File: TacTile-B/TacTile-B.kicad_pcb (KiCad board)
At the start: 2 copper layers, 59.9 x 59.9 mm, 97 parts, among them J1 Conn_01x02, J10 Conn_01x02, J11 Conn_01x02, J12 Conn_01x02, J13 Conn_01x02, J14 Conn_01x02, J15 Conn_01x02, J16 Conn_01x02, J17 Conn_01x02, J2 Conn_01x02, J3 Conn_01x02, J4 Conn_01x02, J5 Conn_01x02, J6 Conn_01x02, J7 Conn_01x02, J8 Conn_01x02, J9 Conn_01x02, U1 MCP14A0304xMNY, U10 MCP14A0304xMNY, U11 MCP14A0304xMNY, U12 MCP14A0304xMNY, U13 MCP14A0304xMNY, U14 MCP14A0304xMNY, U15 MCP14A0304xMNY, U16 MCP14A0304xMNY, U2 MCP14A0304xMNY, U3 MCP14A0304xMNY, U4 MCP14A0304xMNY, U5 MCP14A0304xMNY, U6 MCP14A0304xMNY, U7 MCP14A0304xMNY, U8 MCP14A0304xMNY, U9 MCP14A0304xMNY

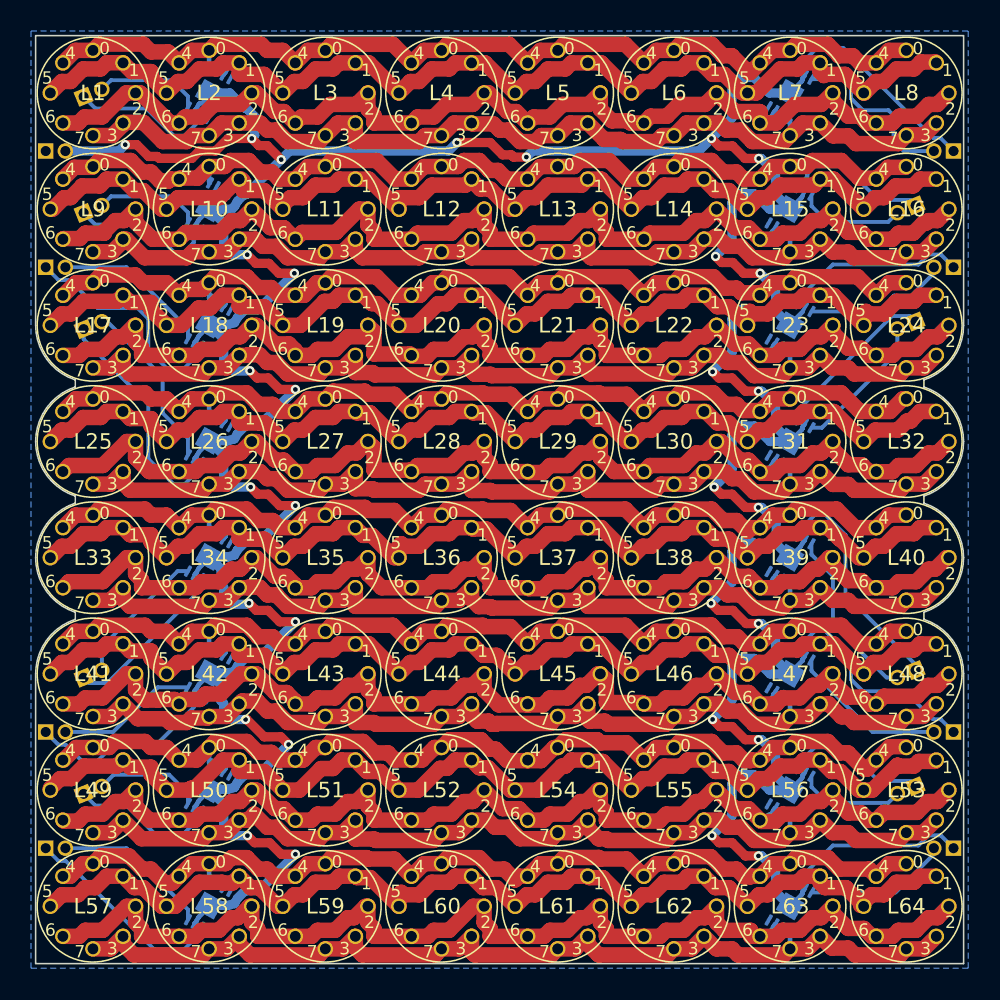
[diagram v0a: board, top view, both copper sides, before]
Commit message: Added photoresistor footprint and enlarged main boards to 60mm
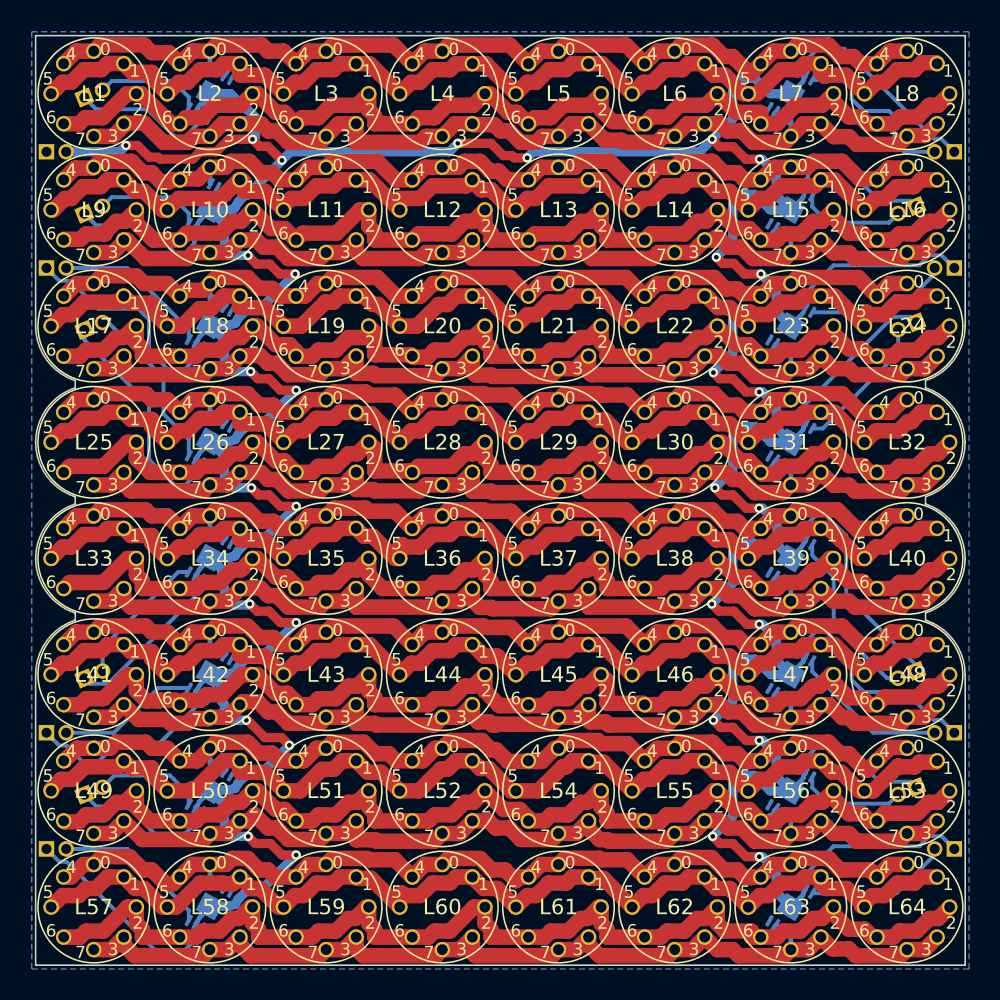
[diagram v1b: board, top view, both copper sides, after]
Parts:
- moved L1 0.07 mm to (28.8, 28.8)
- moved J4 0.07 mm to (81.9, 36.0)
- moved J8 0.07 mm to (81.9, 43.5)
- moved U3 0.07 mm to (36.2, 36.2)
- moved U5 0.07 mm to (36.2, 43.7)
- moved U7 0.07 mm to (36.2, 51.2)
- moved U9 0.07 mm to (36.2, 58.7)
- moved J1 0.07 mm to (28.1, 29.0)
- moved J11 0.07 mm to (25.7, 70.0)
- moved J13 0.07 mm to (28.1, 74.0)
- moved J15 0.07 mm to (25.7, 77.5)
- moved J17 0.07 mm to (25.7, 32.5)
- moved J3 0.07 mm to (28.1, 36.5)
- moved J5 0.07 mm to (25.7, 40.0)
- moved J7 0.07 mm to (28.1, 44.0)
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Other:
- board size 59.9 x 59.9 mm -> 60 x 60 mm
